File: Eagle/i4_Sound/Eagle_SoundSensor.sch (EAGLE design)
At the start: 18 parts, among them U1 LM358DR

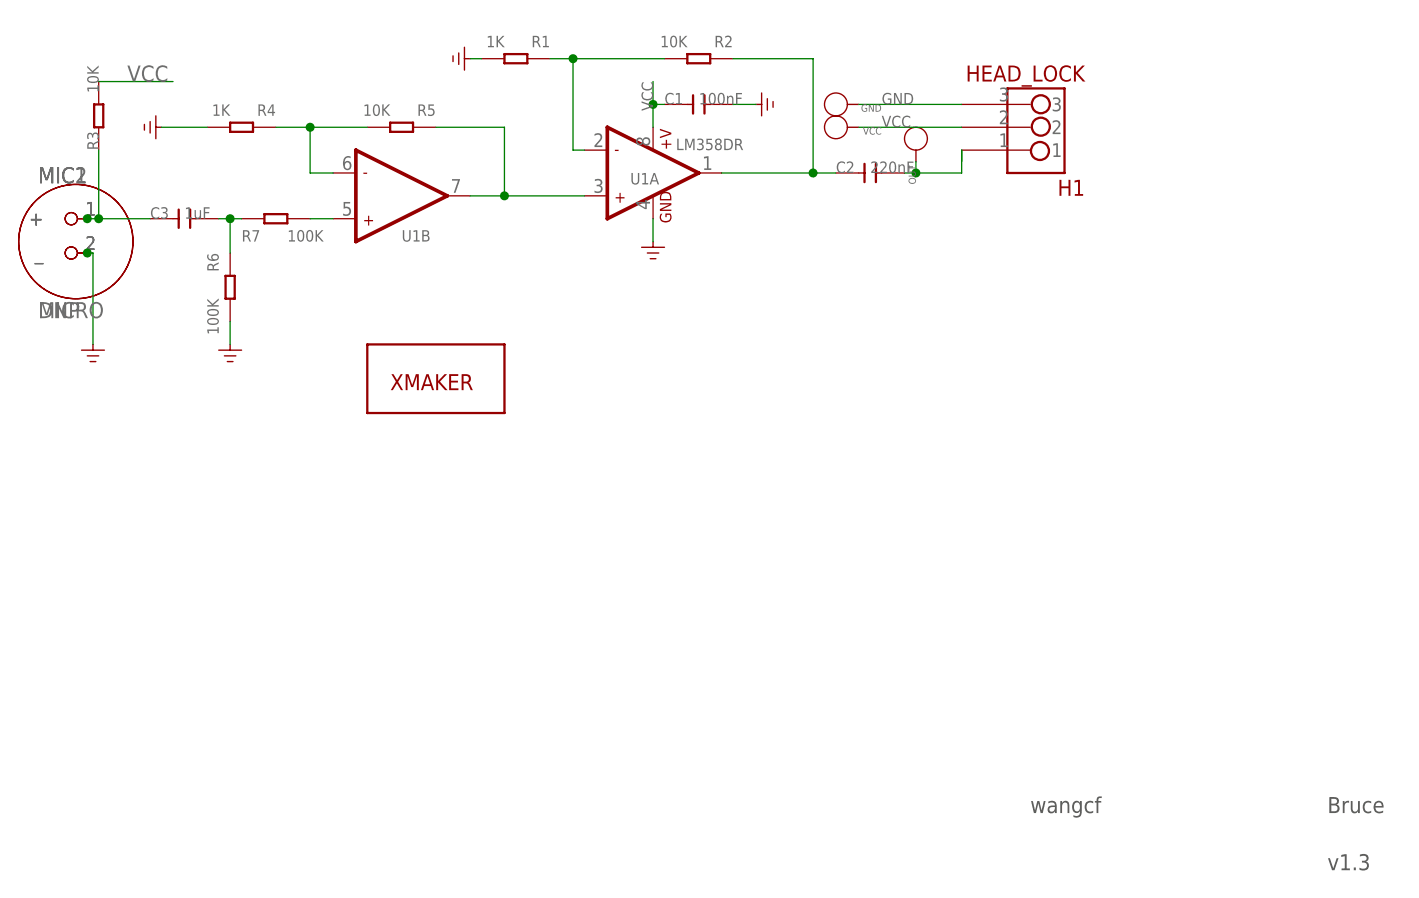
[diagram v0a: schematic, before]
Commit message: 调整蜂鸣器
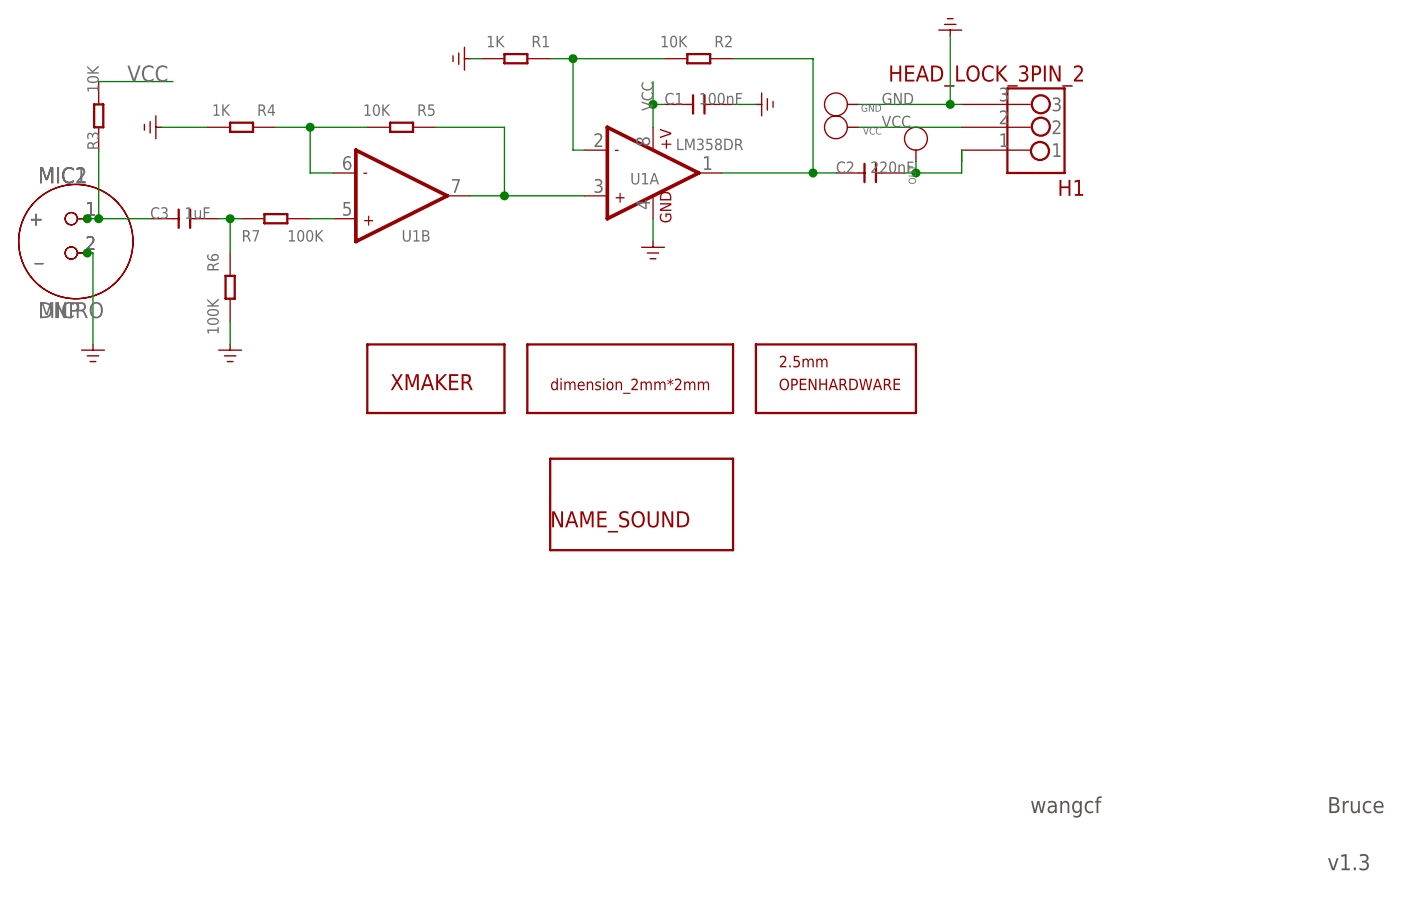
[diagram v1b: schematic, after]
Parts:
- added U$11: DIMENSION_2MM2MM, Xmaker:DIMENSION_2MM2MM
- added U$12: OPENHARDWARE_2.5MM_TOP, Xmaker:OPENHARDWARE_2.5MM_TOP
- added U$13: NAME_SOUND, Xmaker:NAME_SOUND
- H1: value HEAD_LOCK -> HEAD_LOCK_3PIN_2; device HEAD_LOCK:HEAD_LOCK -> Xmaker:HEAD_LOCK_3PIN_2
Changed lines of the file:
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@@
 <?xml version="1.0" encoding="utf-8"?>
 <!DOCTYPE eagle SYSTEM "eagle.dtd">
-<eagle version="6.6.0">
+<eagle version="7.2.0">
 <drawing>
 <settings>
@@
 <setting verticaltext="up"/>
 </settings>
-<grid distance="0.1" unitdist="inch" unit="inch" style="lines" multiple="1" display="no" altdistance="0.01" altunitdist="inch" altunit="inch"/>
+<grid distance="0.01" unitdist="inch" unit="inch" style="lines" multiple="1" display="no" altdistance="0.01" altunitdist="inch" altunit="inch"/>
 <layers>
 <layer number="1" name="Top" color="4" fill="1" visible="no" active="no"/>
@@
 <layer number="54" name="bGND_GNDA" color="1" fill="9" visible="no" active="no"/>
 <layer number="56" name="wert" color="7" fill="1" visible="no" active="no"/>
+<layer number="57" name="tCAD" color="7" fill="1" visible="no" active="no"/>
+<layer number="59" name="tCarbon" color="7" fill="1" visible="no" active="no"/>
+<layer number="60" name="bCarbon" color="7" fill="1" visible="no" active="no"/>
+<layer number="90" name="Modules" color="5" fill="1" visible="no" active="no"/>
 <layer number="91" name="Nets" color="2" fill="1" visible="yes" active="yes"/>
 <layer number="92" name="Busses" color="1" fill="1" visible="yes" active="yes"/>
@@
 <layer number="97" name="Info" color="7" fill="1" visible="yes" active="yes"/>
 <layer number="98" name="Guide" color="6" fill="1" visible="yes" active="yes"/>
+<layer number="99" name="SpiceOrder" color="7" fill="1" visible="no" active="no"/>
 <layer number="100" name="Muster" color="7" fill="1" visible="no" active="no"/>
 <layer number="101" name="Patch_Top" color="12" fill="4" visible="yes" active="yes"/>
@@
 <layer number="111" name="111" color="7" fill="1" visible="no" active="yes"/>
 <layer number="112" name="tSilk" color="7" fill="1" visible="no" active="yes"/>
+<layer number="113" name="IDFDebug" color="7" fill="1" visible="yes" active="yes"/>
 <layer number="116" name="Patch_BOT" color="9" fill="4" visible="yes" active="yes"/>
 <layer number="118" name="Rect_Pads" color="7" fill="1" visible="no" active="yes"/>
@@
 <layer number="127" name="_tValues" color="7" fill="1" visible="no" active="yes"/>
 <layer number="128" name="_bValues" color="7" fill="1" visible="no" active="yes"/>
+<layer number="129" name="Mask" color="7" fill="1" visible="yes" active="yes"/>
 <layer number="131" name="tAdjust" color="7" fill="1" visible="no" active="yes"/>
 <layer number="132" name="bAdjust" color="7" fill="1" visible="no" active="yes"/>
 <layer number="144" name="DrillLegend" color="7" fill="1" visible="no" active="yes"/>
+<layer number="150" name="Notes" color="7" fill="1" visible="yes" active="yes"/>
 <layer number="151" name="HeatSink" color="7" fill="1" visible="yes" active="yes"/>
 <layer number="152" name="_bDocu" color="7" fill="1" visible="no" active="yes"/>
+<layer number="153" name="FabDoc1" color="7" fill="1" visible="yes" active="yes"/>
+<layer number="154" name="FabDoc2" color="7" fill="1" visible="yes" active="yes"/>
+<layer number="155" name="FabDoc3" color="7" fill="1" visible="yes" active="yes"/>
 <layer number="199" name="Contour" color="7" fill="1" visible="no" active="yes"/>
 <layer number="200" name="200bmp" color="1" fill="10" visible="no" active="no"/>
@@
 <layer number="227" name="227bmp" color="7" fill="1" visible="yes" active="yes"/>
 <layer number="228" name="228bmp" color="7" fill="1" visible="yes" active="yes"/>
+<layer number="229" name="229bmp" color="7" fill="1" visible="yes" active="yes"/>
 <layer number="230" name="230bmp" color="7" fill="1" visible="no" active="yes"/>
+<layer number="231" name="231bmp" color="7" fill="1" visible="yes" active="yes"/>
 <layer number="248" name="Housing" color="7" fill="1" visible="no" active="yes"/>
 <layer number="249" name="Edge" color="7" fill="1" visible="no" active="yes"/>
@@
 <layer number="251" name="SMDround" color="12" fill="11" visible="no" active="no"/>
 <layer number="254" name="cooling" color="7" fill="1" visible="yes" active="yes"/>
+<layer number="255" name="routoute" color="7" fill="1" visible="yes" active="yes"/>
 </layers>
 <schematic xreflabel="%F%N/%S.%C%R" xrefpart="/%S.%C%R">
@@
 <part name="C2" library="Discrete" deviceset="C*" device="-0603" value="220nF"/>
 <part name="U$10" library="moudle" deviceset="SEEEDSTUDIO_SCH_FRAME" device=""/>
-<part name="H1" library="HEAD_LOCK" deviceset="HEAD_LOCK" device=""/>
+<part name="H1" library="Xmaker" deviceset="HEAD_LOCK_3PIN_2" device=""/>
 <part name="U$7" library="Xmaker_yuhui" deviceset="XMAKERLOGO" device=""/>
+<part name="U$11" library="Xmaker" deviceset="DIMENSION_2MM*2MM" device=""/>
+<part name="U$12" library="Xmaker" deviceset="OPENHARDWARE_2.5MM_TOP" device=""/>
+<part name="U$13" library="Xmaker" deviceset="NAME_SOUND" device=""/>
+<part name="U$14" library="Power or GND " deviceset="GND_POWER" device=""/>
 </parts>
 <sheets>
@@
 <instance part="C2" gate="C" x="172.72" y="82.55"/>
 <instance part="U$10" gate="G$1" x="0" y="0"/>
-<instance part="H1" gate="G$1" x="195.58" y="95.25" rot="R180"/>
+<instance part="H1" gate="G$1" x="190.5" y="87.63" rot="R180"/>
 <instance part="U$7" gate="G$1" x="124.46" y="58.42"/>
+<instance part="U$11" gate="G$1" x="134.62" y="55.88"/>
+<instance part="U$12" gate="G$1" x="172.72" y="58.42"/>
+<instance part="U$13" gate="G$1" x="147.32" y="45.72"/>
+<instance part="U$14" gate="G$1" x="181.61" y="97.79" rot="R180"/>
 </instances>
 <busses>
@@
 <net name="GND" class="0">
 <segment>
-<wire x1="182.88" y1="90.17" x2="171.45" y2="90.17" width="0.1524" layer="91"/>
+<wire x1="182.88" y1="90.17" x2="181.61" y2="90.17" width="0.1524" layer="91"/>
 <label x="173.99" y="90.17" size="1.27" layer="95" ratio="10"/>
 <pinref part="GND" gate="TP" pin="T"/>
 <pinref part="H1" gate="G$1" pin="3"/>
+<pinref part="U$14" gate="G$1" pin="GND"/>
+<wire x1="181.61" y1="90.17" x2="171.45" y2="90.17" width="0.1524" layer="91"/>
+<wire x1="181.61" y1="97.79" x2="181.61" y2="90.17" width="0.1524" layer="91"/>
+<junction x="181.61" y="90.17"/>
 </segment>
 <segment>
